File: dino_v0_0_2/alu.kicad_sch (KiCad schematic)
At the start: 20 parts, among them U38 74F382N, U40 74F382N, U45 74LS373, U46 74LS373, U47 74LS373, U48 74LS157, U49 74LS273, U50 74LS02, U52 74LS02, U53 74LS08

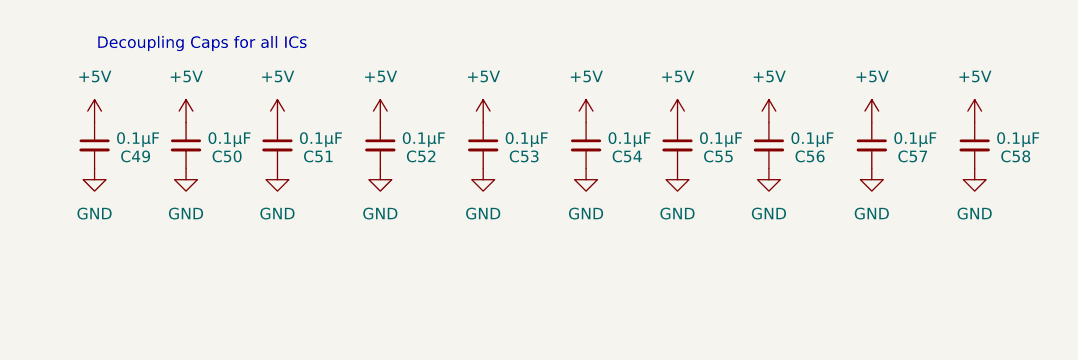
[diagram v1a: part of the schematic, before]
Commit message: feat(dino): generate + stamp per-sheet I/O contracts
Each module's boundary signals (IN/OUT/BIDIR with counterpart sheets)
derived from the kicad-cli netlist and placed as a text block on the
physical sheet, so a bench rig knows exactly what to drive and observe
per board. kicad_contracts.py regenerates both the markdown and the
stamps idempotently; stamping verified electrically neutral.
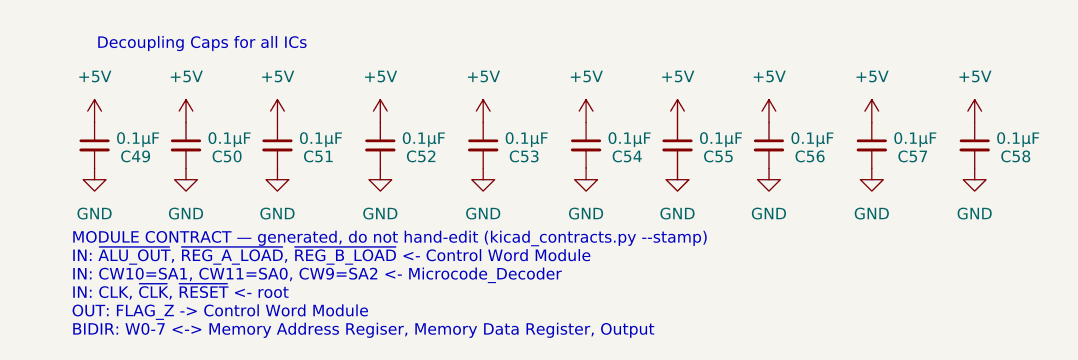
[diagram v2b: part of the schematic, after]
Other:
- note added: "MODULE CONTRACT — generated, do not hand-edit (kicad_contracts.py --stamp) IN: ~{ALU_OUT}, ~{REG_A_LOAD}, ~{REG_B_LOAD} <- Control Word Module IN: CW10=SA1, CW11=SA0, CW9=SA2 <- Microcode_Decoder IN: CLK, ~{CLK}, ~{RESET} <- root OUT: FLAG_Z -> Control Word Module BIDIR: W0-7 <-> Memory Address Regiser, Memory Data Register, Output"
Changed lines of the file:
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@@
+		)
+	)
+	(text "MODULE CONTRACT — generated, do not hand-edit (kicad_contracts.py --stamp)\nIN: ~{ALU_OUT}, ~{REG_A_LOAD}, ~{REG_B_LOAD} <- Control Word Module\nIN: CW10=SA1, CW11=SA0, CW9=SA2 <- Microcode_Decoder\nIN: CLK, ~{CLK}, ~{RESET} <- root\nOUT: FLAG_Z -> Control Word Module\nBIDIR: W0-7 <-> Memory Address Regiser, Memory Data Register, Output"
+		(exclude_from_sim no)
+		(at 15.24 213.2 0)
+		(effects
+			(font
+				(size 1.27 1.27)
+			)
+			(justify left bottom)
 		)
 	)

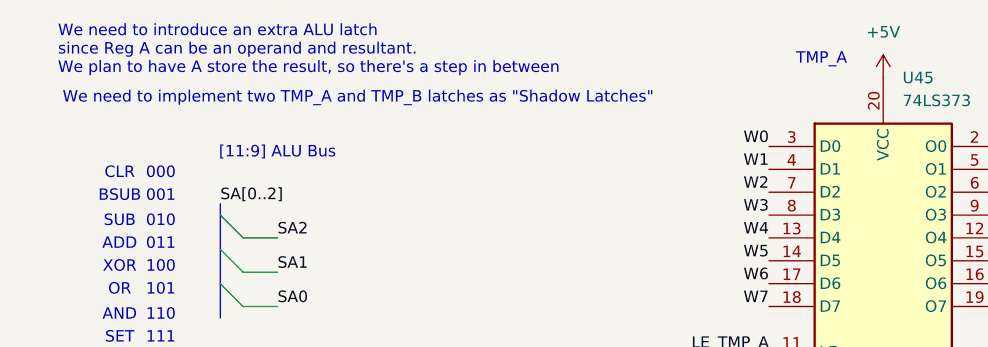
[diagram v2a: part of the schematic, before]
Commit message: fix(dino): three review-found schematic bugs on microcode/memory
- microcode U9/U15: ~WE tied +5V, A12 tied GND (were floating with NC
  flags — in-circuit corruption + image-aliasing hazard on AT28C64B)
- memory: label the U24.~OE/U19.CE net ~{ROM_OUT} — the ROM read path
  had no driver as drawn (caught by new kicad_netlist.py --lint)
- memory: U21 (RAM-side '245) CE now AND(~RAM_OUT, ~WRITE_DIR) via U51
  spare gates — was enabled by ~RAM_EN alone, buffering floating RAM DQ
  onto MDR against register drivers whenever MAR parked on a RAM
  address with no RAM op in flight

Contracts restamped; all verified in kicad_netlist.py + kicad-cli
export; lint clean project-wide.
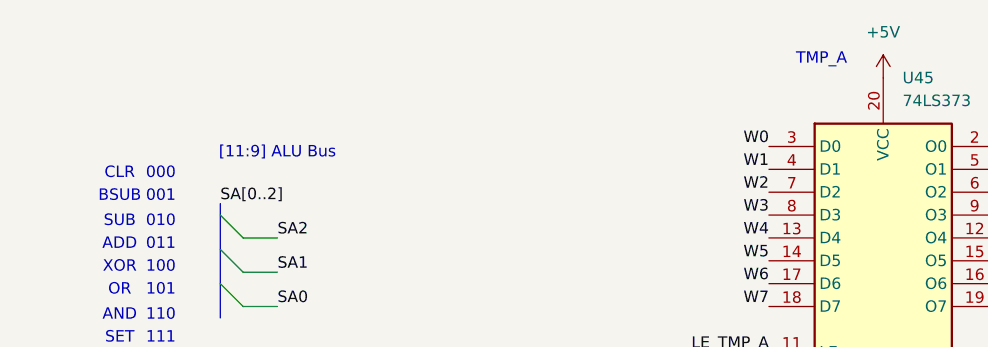
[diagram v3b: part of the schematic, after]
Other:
- note removed: "We need to implement two TMP_A and TMP_B latches as "Shadow Latches""
- note removed: "We need to introduce an extra ALU latch since Reg A can be an operand and resultant. We plan to have A store the result, so there's a step in between"
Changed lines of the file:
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@@
-		)
-	)
-	(text "We need to implement two TMP_A and TMP_B latches as \"Shadow Latches\""
-		(exclude_from_sim no)
-		(at 14.224 26.416 0)
-		(effects
-			(font
-				(size 1.27 1.27)
-			)
-			(justify left)
 		)
 	)
@@
 		)
 	)
-	(text "We need to introduce an extra ALU latch \nsince Reg A can be an operand and resultant. \nWe plan to have A store the result, so there's a step in between\n"
-		(exclude_from_sim no)
-		(at 13.716 21.082 0)
-		(effects
-			(font
-				(size 1.27 1.27)
-			)
-			(justify left)
-		)
-	)
